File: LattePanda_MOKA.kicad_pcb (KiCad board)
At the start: 4 copper layers, 100 x 70.1 mm, 229 parts, among them CN78 SMTWE2055MTJ, CN79 SMTWE2055MTJ, J15 Bus_M.2_Socket_M, J16 Bus_M.2_Socket_E, J3 HDMI_A, J78 I2C, J79 GLPLX-SMT-188S7-QQ-Y_G, J81 I2C, Q1 2N7002, Q2 2SK3018, Q3 2SK3018, Q4 2SK3018, Q8 2N7002, SW101 MK-11C04-G013, SW78 GT-TC193A-H0675-L1, U1 TPAZ1023-04F, U14 CH224K, U15 SY8253ADC, U16 SY8253ADC, U2 TPAZ1023-04F, U33 SHT4x, U34 STCC4, U5 ULC0524P, U6 RTL8111H-CG-RH, U7 ULC0524P, U78 SMTWEM220STR, U79 SMTWEM220STR, U8 ULC0524P, U80 SMTWEM220STR, U81 B4B-PH-SM4-TBT(LF)(SN), Y1 25MHz

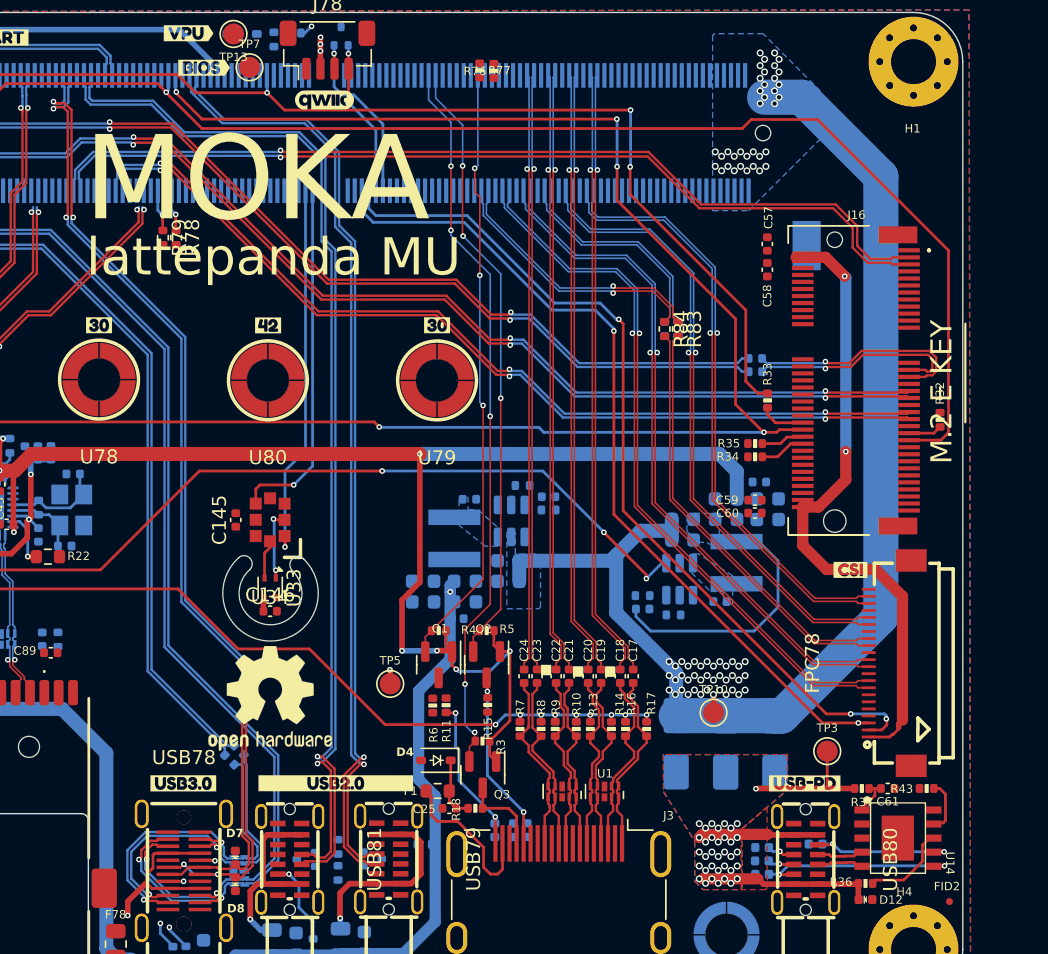
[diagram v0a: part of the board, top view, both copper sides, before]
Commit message: hierarchical schema rework
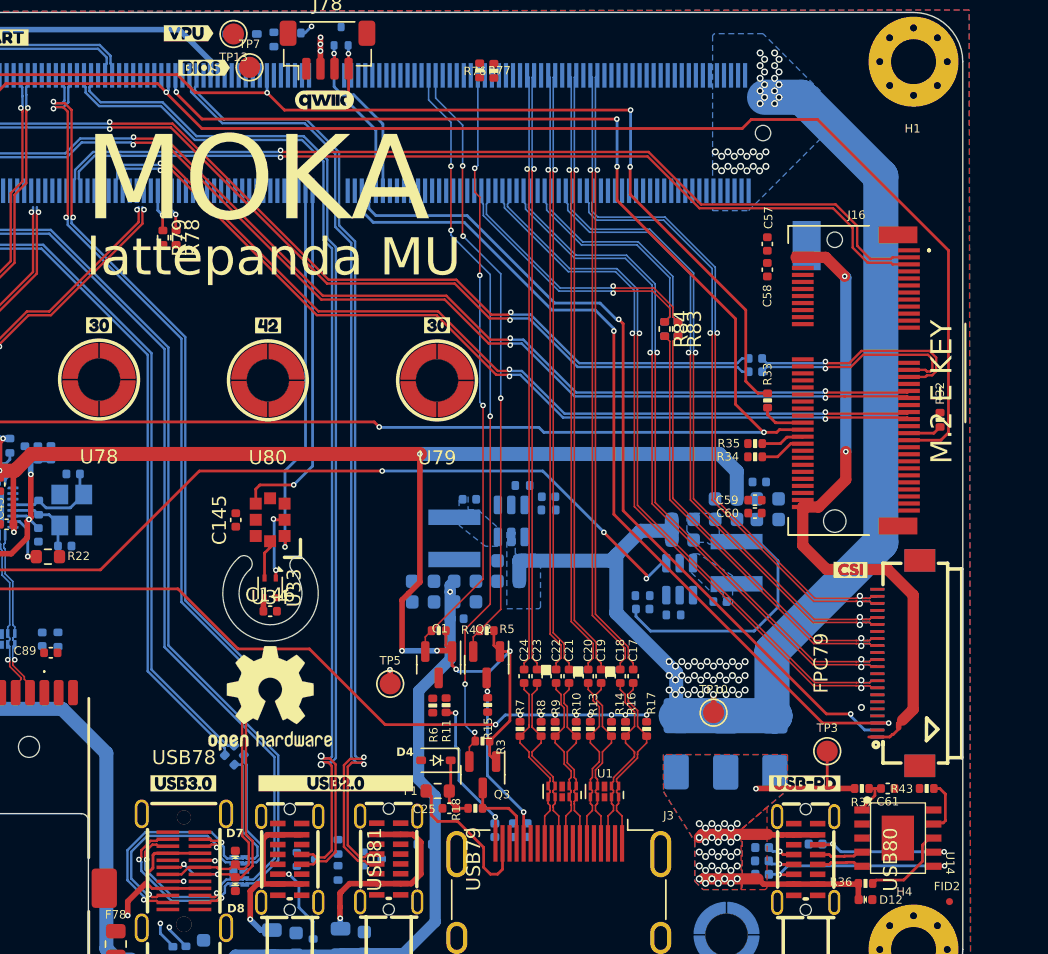
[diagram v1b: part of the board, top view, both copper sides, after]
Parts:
- added FPC79: FH12-22S-0.5SH(55), EasyEDA:FPC-SMD_22P-P0.50_FH12-22S-0.5SH-55, F.Cu at (152.0, 71.9)
- C49, C50, C55, C56: value 220nF/50V -> 220n
- FPC78: moved to B.Cu
- R34, R35: value 10K/1% -> 10K
- moved FPC78 0.61 mm to (152.0, 71.9), turned to -90 degrees
- turned D83 to 0 degrees
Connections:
- net /CSI/CSI_C_CK+ renamed /CSI/CSI_C.CK+
- net /CSI/CSI_C_CK- renamed /CSI/CSI_C.CK-
- net /CSI/CSI_D_CK+ renamed /CSI/CSI_D.CK+
- net /CSI/CSI_D_CK- renamed /CSI/CSI_D.CK-
- net /GPIO/SOC_UART0_RX renamed /LattePanda Module/SOC_UART0_RX
- net /GPIO/SOC_UART0_TX renamed /LattePanda Module/SOC_UART0_TX
- net /GPIO/SOC_UART1_RX renamed /LattePanda Module/SOC_UART1_RX
- net /GPIO/SOC_UART1_TX renamed /LattePanda Module/SOC_UART1_TX
- net /GPIO/SOC_UART2_RX renamed /LattePanda Module/SOC_UART2_RX
- net /GPIO/SOC_UART2_TX renamed /LattePanda Module/SOC_UART2_TX
- net /I2C5_SCL renamed /LattePanda Module/I2C5_SCL
- net /I2C5_SDA renamed /LattePanda Module/I2C5_SDA
- net /LattePanda Module/HSIO_0_TX+ renamed /LattePanda Module/USB3_2.TX+
- net /LattePanda Module/HSIO_0_TX- renamed /LattePanda Module/USB3_2.TX-
- net /LattePanda Module/HSIO_2_RX+ renamed /LattePanda Module/PCIE_2.RX+
- net /LattePanda Module/HSIO_2_RX- renamed /LattePanda Module/PCIE_2.RX-
- net /LattePanda Module/HSIO_2_TX+ renamed /LattePanda Module/PCIE_2.TX+
- net /LattePanda Module/HSIO_2_TX- renamed /LattePanda Module/PCIE_2.TX-
- net /LattePanda Module/HSIO_3_RX+ renamed /LattePanda Module/PCIE_3.RX+
- net /LattePanda Module/HSIO_3_RX- renamed /LattePanda Module/PCIE_3.RX-
- net /LattePanda Module/HSIO_3_TX+ renamed /LattePanda Module/PCIE_3.TX+
- net /LattePanda Module/HSIO_3_TX- renamed /LattePanda Module/PCIE_3.TX-
- net /LattePanda Module/USB_2_P1+ renamed /LattePanda Module/USB_2.P1+
- net /LattePanda Module/USB_2_P1- renamed /LattePanda Module/USB_2.P1-
- net /LattePanda Module/USB_2_P7+ renamed /LattePanda Module/PCIE_3.P+
- net /LattePanda Module/USB_2_P7- renamed /LattePanda Module/PCIE_3.P-
- net /USB2.0&USB3.0/CON_USB1_D_N renamed /LattePanda Module/USB2_5.P-
- net /USB2.0&USB3.0/CON_USB1_D_P renamed /LattePanda Module/USB2_5.P+
- net /USB2.0&USB3.0/CON_USB2_D_N renamed /LattePanda Module/USB2_3.P-
- net /USB2.0&USB3.0/CON_USB2_D_P renamed /LattePanda Module/USB2_3.P+
- net /USB2.0&USB3.0/CON_USB3_D_N renamed /LattePanda Module/USB3_2.P-
- net /USB2.0&USB3.0/CON_USB3_D_P renamed /LattePanda Module/USB3_2.P+
- net /USB2.0&USB3.0/CON_USB3_SSRX_N renamed /LattePanda Module/USB3_2.RX-
- net /USB2.0&USB3.0/CON_USB3_SSRX_P renamed /LattePanda Module/USB3_2.RX+
- net /~{WAKE} renamed /LattePanda Module/~{PEWAKE}
- A1 pad 190: /CSI/CSI_C_D2+ -> /CSI/CSI_C.D2+
- A1 pad 192: /CSI/CSI_C_D2- -> /CSI/CSI_C.D2-
- A1 pad 196: /CSI/CSI_C_D3+ -> /CSI/CSI_C.D3+
- A1 pad 197: /HDMI/DDI_B_TX3- -> /LattePanda Module/DDI_B_TX3-
- A1 pad 198: /CSI/CSI_C_D3- -> /CSI/CSI_C.D3-
- A1 pad 199: /HDMI/DDI_B_TX3+ -> /LattePanda Module/DDI_B_TX3+
- A1 pad 203: /HDMI/DDI_B_TX2- -> /LattePanda Module/DDI_B_TX2-
- A1 pad 205: /HDMI/DDI_B_TX2+ -> /LattePanda Module/DDI_B_TX2+
- A1 pad 208: /CSI/CSI_C_D1+ -> /CSI/CSI_C.D1+
- A1 pad 209: /HDMI/DDI_B_TX1- -> /LattePanda Module/DDI_B_TX1-
- A1 pad 210: /CSI/CSI_C_D1- -> /CSI/CSI_C.D1-
- A1 pad 211: /HDMI/DDI_B_TX1+ -> /LattePanda Module/DDI_B_TX1+
- A1 pad 214: /CSI/CSI_C_D0+ -> /CSI/CSI_C.D0+
- A1 pad 215: /HDMI/DDI_B_TX0- -> /LattePanda Module/DDI_B_TX0-
- A1 pad 216: /CSI/CSI_C_D0- -> /CSI/CSI_C.D0-
- A1 pad 217: /HDMI/DDI_B_TX0+ -> /LattePanda Module/DDI_B_TX0+
- A1 pad 61: /Gigabit Ethernet/GbE_PCIe_TX+ -> /LattePanda Module/GBE.TX+
- A1 pad 63: /Gigabit Ethernet/GbE_PCIe_TX- -> /LattePanda Module/GBE.TX-
- A1 pad 64: /Gigabit Ethernet/GbE_PCIe_RX+ -> /LattePanda Module/GBE.RX+
- A1 pad 66: /Gigabit Ethernet/GbE_PCIe_RX- -> /LattePanda Module/GBE.RX-
- A1 pad 85: /LattePanda Module/REFCLK0+ -> /LattePanda Module/PCIE_2.CK0+
- A1 pad 87: /LattePanda Module/REFCLK0- -> /LattePanda Module/PCIE_2.CK0-
- A1 pad 88: /LattePanda Module/REFCLK3+ -> /LattePanda Module/PCIE_3.CK3+
- A1 pad 90: /LattePanda Module/REFCLK3- -> /LattePanda Module/PCIE_3.CK3-
- A1 pad 94: /Gigabit Ethernet/GbE_PCIe_CLK+ -> /LattePanda Module/GBE.CK+
- A1 pad 96: /Gigabit Ethernet/GbE_PCIe_CLK- -> /LattePanda Module/GBE.CK-
- C38 pad 2: /Gigabit Ethernet/GbE_PCIe_TX- -> /Gigabit Ethernet/GBE.TX-
- C39 pad 2: /Gigabit Ethernet/GbE_PCIe_RX- -> /Gigabit Ethernet/GBE.RX-
- C42 pad 2: /Gigabit Ethernet/GbE_PCIe_TX+ -> /Gigabit Ethernet/GBE.TX+
- C43 pad 2: /Gigabit Ethernet/GbE_PCIe_RX+ -> /Gigabit Ethernet/GBE.RX+
- C49 pad 2: /M.2 E&M Key/CON_PCIE_TX_1+ -> /M.2 E&M Key/TX+
- C50 pad 2: /M.2 E&M Key/CON_PCIE_TX_1- -> /M.2 E&M Key/TX-
- C55 pad 2: /M.2 E&M Key/CON_PCIE_TX_0+ -> /M.2 E&M Key/TX+
- C56 pad 2: /M.2 E&M Key/CON_PCIE_TX_0- -> /M.2 E&M Key/TX-
- FPC78 pad 1: +3V3 -> GND
- FPC78 pad 11: /CSI/CSI_C_D3+ -> /CSI/CSI_C.D3-
- FPC78 pad 12: /CSI/CSI_C_D3- -> /CSI/CSI_C.D3+
- FPC78 pad 14: /CSI/CSI_CK+ -> /CSI/CSI_C.D2-
- FPC78 pad 15: /CSI/CSI_CK- -> /CSI/CSI_C.D2+
- FPC78 pad 17: /CSI/CSI_C_D1+ -> /CSI/CAM_GPIO0
- FPC78 pad 18: /CSI/CSI_C_D1- -> /CSI/CAM_GPIO0
- FPC78 pad 2: /I2C3_SDA -> /CSI/CSI_C.D0-
- FPC78 pad 20: /CSI/CSI_C_D0+ -> /I2C3_SCL
- FPC78 pad 21: /CSI/CSI_C_D0- -> /I2C3_SDA
- FPC78 pad 22: GND -> +3V3
- FPC78 pad 3: /I2C3_SCL -> /CSI/CSI_C.D0+
- FPC78 pad 5: /CSI/CAM_GPIO1 -> /CSI/CSI_C.D1-
- FPC78 pad 6: /CSI/CAM_GPIO0 -> /CSI/CSI_C.D1+
- FPC78 pad 8: /CSI/CSI_C_D2+ -> /CSI/CSI_CK-
- FPC78 pad 9: /CSI/CSI_C_D2- -> /CSI/CSI_CK+
- J15 pad 47: /M.2 E&M Key/CON_PCIE_TX_1- -> /M.2 E&M Key/TX-
- J15 pad 49: /M.2 E&M Key/CON_PCIE_TX_1+ -> /M.2 E&M Key/TX+
- J15 pad 53: /LattePanda Module/REFCLK0+ -> /LattePanda Module/PCIE_2.CKE-
- J15 pad 55: /LattePanda Module/REFCLK0- -> /LattePanda Module/PCIE_2.CKE+
- J16 pad 35: /M.2 E&M Key/CON_PCIE_TX_0+ -> /M.2 E&M Key/TX+
- J16 pad 37: /M.2 E&M Key/CON_PCIE_TX_0- -> /M.2 E&M Key/TX-
- J16 pad 47: /LattePanda Module/REFCLK3+ -> /LattePanda Module/PCIE_3.CKE+
- J16 pad 49: /LattePanda Module/REFCLK3- -> /LattePanda Module/PCIE_3.CKE-
- U6 pad 15: /Gigabit Ethernet/GbE_PCIe_CLK+ -> /Gigabit Ethernet/GBE.CK+
- U6 pad 16: /Gigabit Ethernet/GbE_PCIe_CLK- -> /Gigabit Ethernet/GBE.CK-
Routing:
- net (no net): track 0.00 -> 307.3 mm, vias 0 -> 12
- net /LattePanda Module/REFCLK3+: track 65.5 -> 0.00 mm, vias 3 -> 0
- net /LattePanda Module/REFCLK3-: track 65.1 -> 0.00 mm, vias 3 -> 0
- net /LattePanda Module/REFCLK0-: track 52.9 -> 0.00 mm, vias 1 -> 0
- net /LattePanda Module/REFCLK0+: track 52.5 -> 0.00 mm, vias 1 -> 0
- net /CSI/CSI_C.D2+: track 0.00 -> 52.4 mm, vias 0 -> 2
- net /CSI/CSI_C.D2-: track 0.00 -> 52.1 mm, vias 0 -> 2
- net /CSI/CSI_C.D3+: track 0.00 -> 50.5 mm, vias 0 -> 2
- net /CSI/CSI_C_D2+: track 50.4 -> 0.00 mm, vias 1 -> 0
- net /CSI/CSI_C.D3-: track 0.00 -> 50.1 mm, vias 0 -> 2
- net /CSI/CSI_C_D2-: track 50.1 -> 0.00 mm, vias 1 -> 0
- net /CSI/CSI_C_D3+: track 48.5 -> 0.00 mm, vias 1 -> 0
- net /CSI/CSI_C_D3-: track 48.1 -> 0.00 mm, vias 1 -> 0
- net /CSI/CSI_C.D1+: track 0.00 -> 46.7 mm, vias 0 -> 2
- net /CSI/CSI_C.D1-: track 0.00 -> 46.3 mm, vias 0 -> 2
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
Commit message: save
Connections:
- C49 pad 2: /M.2 E&M Key/TX+ -> /M.2 E&M Key/M_TX+
- C50 pad 2: /M.2 E&M Key/TX- -> /M.2 E&M Key/M_TX-
- C55 pad 2: /M.2 E&M Key/TX+ -> /M.2 E&M Key/E_TX+
- C56 pad 2: /M.2 E&M Key/TX- -> /M.2 E&M Key/E_TX-
- FPC78 pad 18: /CSI/CAM_GPIO0 -> /CSI/CAM_GPIO1
- FPC79 pad 5: /CSI/CAM_GPIO0 -> /CSI/CAM_GPIO1
- J15 pad 47: /M.2 E&M Key/TX- -> /M.2 E&M Key/M_TX-
- J15 pad 49: /M.2 E&M Key/TX+ -> /M.2 E&M Key/M_TX+
- J16 pad 35: /M.2 E&M Key/TX+ -> /M.2 E&M Key/E_TX+
- J16 pad 37: /M.2 E&M Key/TX- -> /M.2 E&M Key/E_TX-
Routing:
- net /M.2 E&M Key/TX-: track 29.0 -> 0.00 mm, vias 1 -> 0
- net /M.2 E&M Key/TX+: track 28.1 -> 0.00 mm, vias 1 -> 0
- net /M.2 E&M Key/E_TX-: track 0.00 -> 16.2 mm, vias 0 -> 1
- net /M.2 E&M Key/E_TX+: track 0.00 -> 15.3 mm, vias 0 -> 1
- net /M.2 E&M Key/M_TX-: track 0.00 -> 12.7 mm
- net /M.2 E&M Key/M_TX+: track 0.00 -> 12.7 mm
